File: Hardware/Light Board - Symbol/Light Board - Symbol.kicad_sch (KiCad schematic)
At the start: 18 parts, among them J1 V+, J2 V-

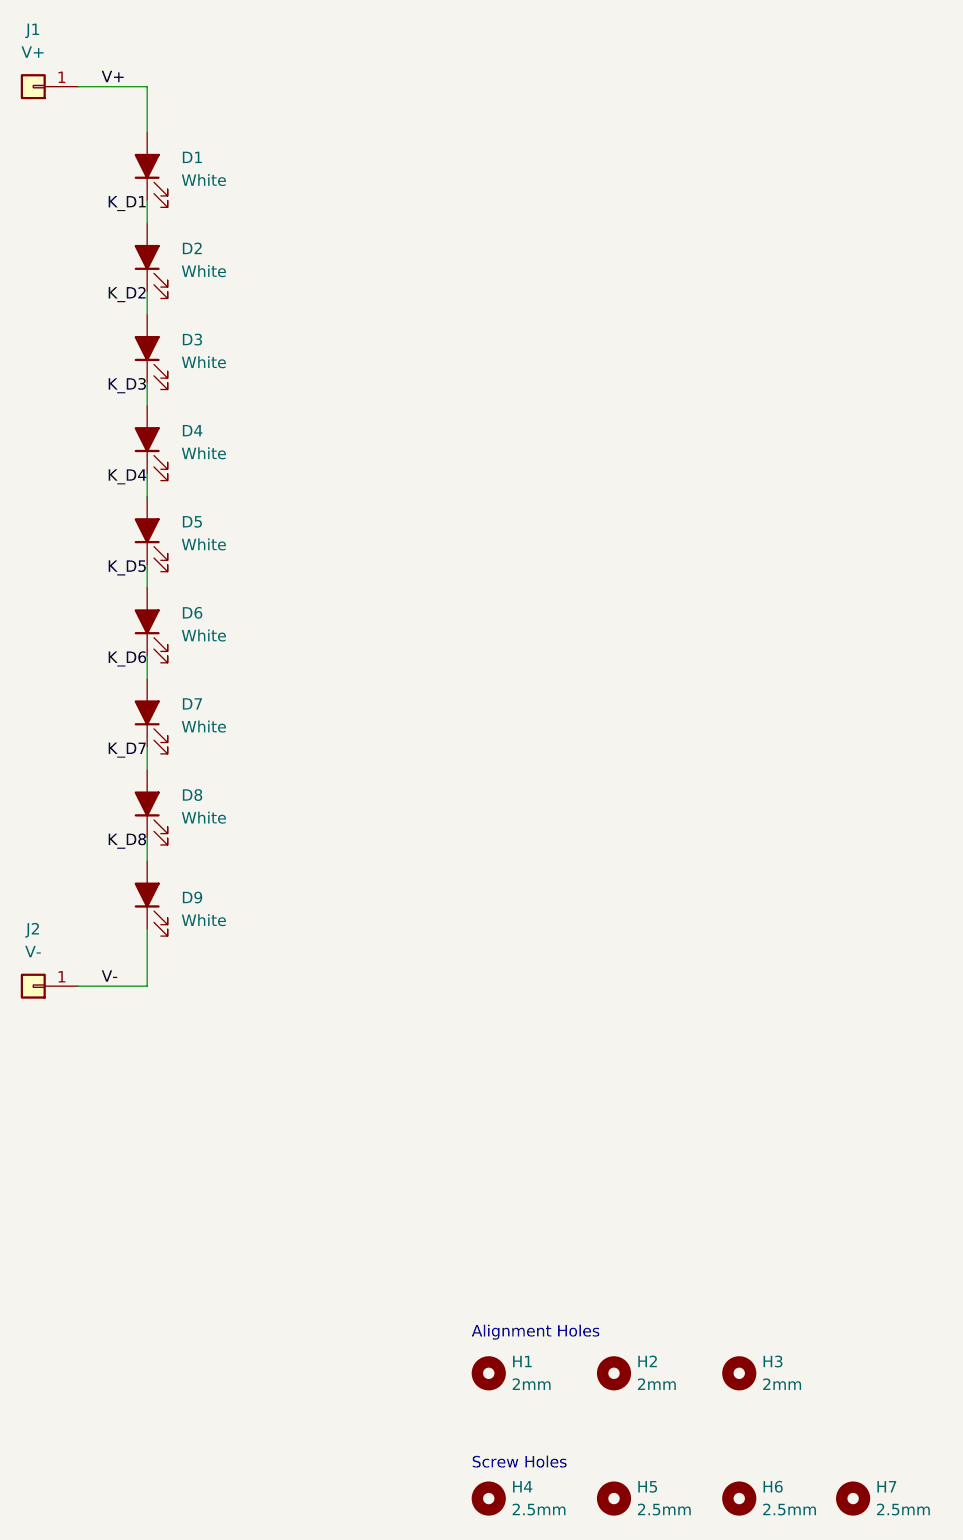
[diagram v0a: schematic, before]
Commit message: Added LED library and fixed orientation
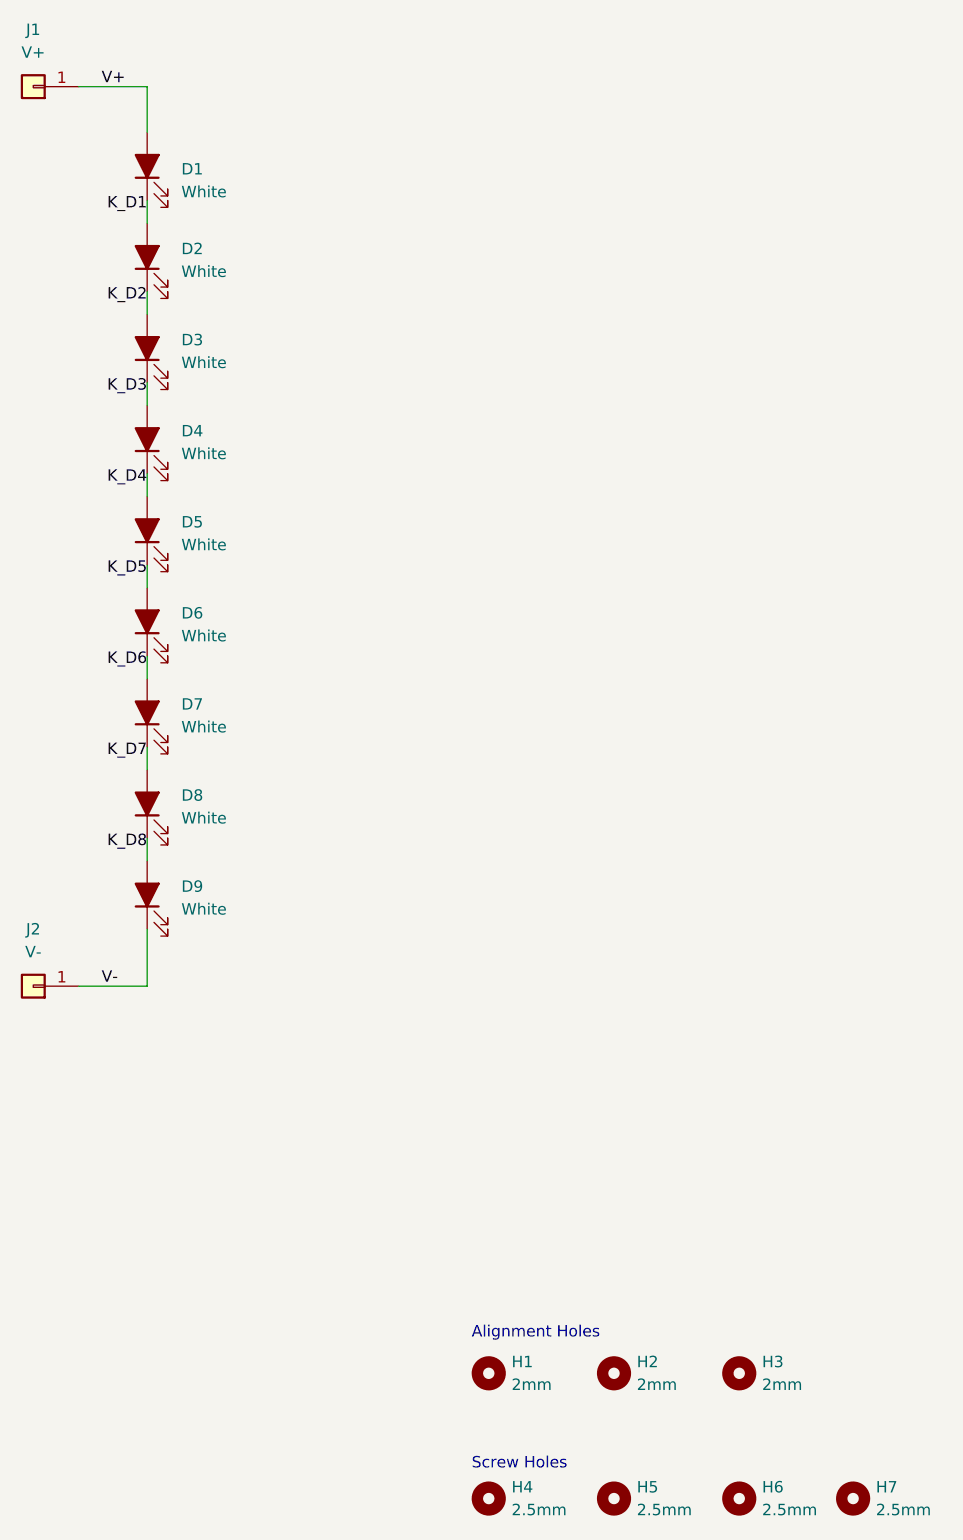
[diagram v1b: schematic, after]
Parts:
- D1: renamed from D9; footprint LED_SMD:LED_Everlight-SMD3528_3.5x2.8mm_67-21ST -> irex_LED_SMD:LED_Cree_J-Series_SMD2835_2.8x3.5mm
- D2: renamed from D8; footprint LED_SMD:LED_Everlight-SMD3528_3.5x2.8mm_67-21ST -> irex_LED_SMD:LED_Cree_J-Series_SMD2835_2.8x3.5mm
- D3: renamed from D7; footprint LED_SMD:LED_Everlight-SMD3528_3.5x2.8mm_67-21ST -> irex_LED_SMD:LED_Cree_J-Series_SMD2835_2.8x3.5mm
- D4: renamed from D6; footprint LED_SMD:LED_Everlight-SMD3528_3.5x2.8mm_67-21ST -> irex_LED_SMD:LED_Cree_J-Series_SMD2835_2.8x3.5mm
- D5: footprint LED_SMD:LED_Everlight-SMD3528_3.5x2.8mm_67-21ST -> irex_LED_SMD:LED_Cree_J-Series_SMD2835_2.8x3.5mm
- D6: renamed from D4; footprint LED_SMD:LED_Everlight-SMD3528_3.5x2.8mm_67-21ST -> irex_LED_SMD:LED_Cree_J-Series_SMD2835_2.8x3.5mm
- D7: renamed from D3; footprint LED_SMD:LED_Everlight-SMD3528_3.5x2.8mm_67-21ST -> irex_LED_SMD:LED_Cree_J-Series_SMD2835_2.8x3.5mm
- D8: renamed from D2; footprint LED_SMD:LED_Everlight-SMD3528_3.5x2.8mm_67-21ST -> irex_LED_SMD:LED_Cree_J-Series_SMD2835_2.8x3.5mm
- D9: renamed from D1; footprint LED_SMD:LED_Everlight-SMD3528_3.5x2.8mm_67-21ST -> irex_LED_SMD:LED_Cree_J-Series_SMD2835_2.8x3.5mm
- J1: renamed from J2; value V- -> V+
- J2: renamed from J1; value V+ -> V-
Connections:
- net K_D1: now also D1.1 (K), D2.2 (A); no longer D8.2 (A), D9.1 (K)
- net K_D2: now also D2.1 (K), D3.2 (A); no longer D7.2 (A), D8.1 (K)
- net K_D3: now also D3.1 (K), D4.2 (A); no longer D6.2 (A), D7.1 (K)
- net K_D4: now also D4.1 (K); no longer D6.1 (K)
- net K_D5: now also D6.2 (A); no longer D4.2 (A)
- net K_D6: now also D6.1 (K), D7.2 (A); no longer D3.2 (A), D4.1 (K)
- net K_D7: now also D7.1 (K), D8.2 (A); no longer D2.2 (A), D3.1 (K)
- net K_D8: now also D8.1 (K), D9.2 (A); no longer D1.2 (A), D2.1 (K)
- net V+: now also D1.2 (A), J1.1 (Pin_1); no longer D9.2 (A), J2.1 (Pin_1)
- net V-: now also D9.1 (K), J2.1 (Pin_1); no longer D1.1 (K), J1.1 (Pin_1)
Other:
- moved on the sheet: D1, D2, D3, D4, D6, D7, D8, D9, J1, J2
